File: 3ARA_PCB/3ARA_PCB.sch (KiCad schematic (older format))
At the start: 45 parts, among them J1 ST-LINK V2, SW1 SW_SPST, SW2 SW_SPST, U1 STM32F407VGTx, Y1 8MHz

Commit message: Continuacion del esquematico
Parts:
- added C20: 100uF, Capacitor_SMD:CP_Elec_6.3x5.4, symbol Device:CP
- added C21: 1000uF, symbol Device:CP
- added D4: MBR360, Diode_SMD:D_SMA_Handsoldering, symbol Diode:MBR340
- added J12: JUMP_1, Connector_PinHeader_2.54mm:PinHeader_1x02_P2.54mm_Vertical, symbol Connector:Conn_01x02_Male
- added J13: JUMP_2, Connector_PinHeader_2.54mm:PinHeader_1x02_P2.54mm_Vertical, symbol Connector:Conn_01x02_Male
- added J14: SPI 1, Connector_JST:JST_EH_B4B-EH-A_1x04_P2.50mm_Vertical, symbol Connector:Conn_01x04_Male
- added J15: UART 5, Connector_JST:JST_EH_B4B-EH-A_1x04_P2.50mm_Vertical, symbol Connector:Conn_01x04_Male
- added J9: DC Input, symbol Connector:Conn_01x02_Male
- added L1: 100uH, Inductor_THT:L_Axial_L7.0mm_D3.3mm_P12.70mm_Horizontal_Fastron_MICC, symbol pspice:INDUCTOR
- added R10, R11, R8, R9: 1K, Resistor_SMD:R_0805_2012Metric_Pad1.20x1.40mm_HandSolder, symbol Device:R_Small
- added U3: LM2576S-3.3, Package_TO_SOT_SMD:TO-263-5_TabPin3, symbol Regulator_Switching:LM2576S-3.3
- C1, C10, C11, C12, C13, C14, C15, C16, C17, C18, C19, C2, C4, C6, C7, C8, C9: footprint (none) -> Capacitor_SMD:C_0805_2012Metric_Pad1.18x1.45mm_HandSolder
- C3, C5: footprint (none) -> Capacitor_THT:C_Disc_D5.0mm_W2.5mm_P5.00mm
- D1, D2: footprint (none) -> LED_SMD:LED_0805_2012Metric_Pad1.15x1.40mm_HandSolder
- D3: renamed from D?; footprint (none) -> LED_SMD:LED_0805_2012Metric_Pad1.15x1.40mm_HandSolder
- J1: footprint (none) -> Connector_PinHeader_2.54mm:PinHeader_2x05_P2.54mm_Vertical
- J10: renamed from J?; value Hall 2 -> Encoder 2; footprint (none) -> Connector_JST:JST_EH_B4B-EH-A_1x04_P2.50mm_Vertical
- J11: renamed from J?; value Hall 3 -> Encoder 3; footprint (none) -> Connector_JST:JST_EH_B4B-EH-A_1x04_P2.50mm_Vertical
- J2, J4, J6: renamed from J?; footprint (none) -> Connector_JST:JST_EH_B3B-EH-A_1x03_P2.50mm_Vertical
- J3, J5, J7: renamed from J?; footprint (none) -> Connector_PinHeader_2.54mm:PinHeader_1x03_P2.54mm_Vertical
- J8: renamed from J?; value Hall 1 -> Encoder 1; footprint (none) -> Connector_JST:JST_EH_B4B-EH-A_1x04_P2.50mm_Vertical
- R1, R2, R3, R4, R5: footprint (none) -> Resistor_SMD:R_0805_2012Metric_Pad1.20x1.40mm_HandSolder
- R6: renamed from R?; value 2K -> 1K; footprint (none) -> Resistor_SMD:R_0805_2012Metric_Pad1.20x1.40mm_HandSolder
- R7: renamed from R?; footprint (none) -> Resistor_SMD:R_0805_2012Metric_Pad1.20x1.40mm_HandSolder
- SW1: value SW_SPST -> RESET; footprint (none) -> Button_Switch_THT:SW_PUSH_6mm
- SW2: value SW_SPST -> BTN; footprint (none) -> Button_Switch_THT:SW_PUSH_6mm
- SW3: renamed from SW?; footprint (none) -> Button_Switch_THT:SW_PUSH_6mm
- U2: renamed from U?; footprint XCVR_HC-05 -> HC05:XCVR_HC-05
- Y1: footprint (none) -> Crystal:Crystal_HC49-U_Vertical
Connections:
- net +3V3: now also C21.1, J15.1 (Pin_1), L1.2, R10.2, R8.2, R9.2, U3.4 (FB)
- net GND: now also C20.2, C21.2, D4.2 (A), J14.4 (Pin_4), J15.4 (Pin_4), J9.2 (Pin_2), U3.3 (GND), U3.5 (~ON~/OFF)
- net HALL_1: now also R8.1
- net HALL_2: now also U1.87 (PD6), R9.1; no longer U1.90 (PB4)
- net HALL_3: now also U1.86 (PD5), R10.1; no longer U1.91 (PB5)
- net MOTOR_2_L: now also U1.3 (PE4)
- net MOTOR_2_R: now also U1.1 (PE2)
- net PA2(Tx): now also J12.1 (Pin_1); no longer U2.2 (UART-RX)
- net PA3(Rx): now also J12.2 (Pin_2); no longer U2.1 (UART-TX)
- net PA5_SPI_1_SCK: now reaches U1.30 (PA5)
- net PA5_SPI_1_SCK: now also J14.3 (Pin_3)
- net PC12_UART_5_Tx: now reaches U1.80 (PC12)
- net PC12_UART_5_Tx: now also J15.3 (Pin_3)
- net PD2_UART_5_Rx: now reaches U1.83 (PD2)
- net PD2_UART_5_Rx: now also J15.2 (Pin_2)
- net at R6.2: now also R11.1; no longer D3.2 (A)
- new net: D3.2 (A), R11.2
- new net: D4.1 (K), L1.1, U3.2 (OUT)
- new net +12V: C20.1, J9.1 (Pin_1), U3.1 (VIN)
- new net HC05_RX: J13.2 (Pin_2), U2.2 (UART-RX)
- new net HC05_TX: J13.1 (Pin_1), U2.1 (UART-TX)
- new net PB4_SPI_1_MISO: J14.2 (Pin_2), U1.90 (PB4)
- new net PB5_SPI_1_MOSI: J14.1 (Pin_1), U1.91 (PB5)
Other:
- note added: "JUMPER"
- note added: "Power Supply"
- moved on the sheet: C18, C19, D1, D2, D3, J1, J10, J11, J8, R2, R3, R4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

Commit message: Avance con el PCB
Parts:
- removed C14: 100nF, Capacitor_SMD:C_0805_2012Metric_Pad1.18x1.45mm_HandSolder, symbol Device:C
- removed C15: 1uF, Capacitor_SMD:C_0805_2012Metric_Pad1.18x1.45mm_HandSolder, symbol Device:C
- added D5, D6: LED, LED_SMD:LED_0805_2012Metric_Pad1.15x1.40mm_HandSolder, symbol Device:LED
- added J16: GPIO, Connector_PinHeader_2.54mm:PinHeader_2x05_P2.54mm_Vertical, symbol Connector_Generic:Conn_02x05_Counter_Clockwise
- added L2: 100uH - optional, Inductor_THT:L_Axial_L7.0mm_D3.3mm_P12.70mm_Horizontal_Fastron_MICC, symbol pspice:INDUCTOR
- added R12, R13, R14: 1K, Resistor_SMD:R_0805_2012Metric_Pad1.20x1.40mm_HandSolder, symbol Device:R_Small
- C18, C19: value 0.1uF -> 100nF
- C21: footprint (none) -> Capacitor_THT:CP_Radial_D10.0mm_P7.50mm
- J1: footprint Connector_PinHeader_2.54mm:PinHeader_2x05_P2.54mm_Vertical -> Connector_IDC:IDC-Header_2x05_P2.54mm_Vertical
- J14: value SPI 1 -> I2C 1
- J3: value Hall 1 -> Hall 3; footprint Connector_PinHeader_2.54mm:PinHeader_1x03_P2.54mm_Vertical -> Connector_JST:JST_EH_B3B-EH-A_1x03_P2.50mm_Vertical
- J5: footprint Connector_PinHeader_2.54mm:PinHeader_1x03_P2.54mm_Vertical -> Connector_JST:JST_EH_B3B-EH-A_1x03_P2.50mm_Vertical
- J7: value Hall 3 -> Hall 1; footprint Connector_PinHeader_2.54mm:PinHeader_1x03_P2.54mm_Vertical -> Connector_JST:JST_EH_B3B-EH-A_1x03_P2.50mm_Vertical
- J9: footprint (none) -> Connector_JST:JST_EH_B2B-EH-A_1x02_P2.50mm_Vertical
- L1: footprint Inductor_THT:L_Axial_L7.0mm_D3.3mm_P12.70mm_Horizontal_Fastron_MICC -> Inductor_SMD:L_12x12mm_H6mm
- R1: value 47 -> 120
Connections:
- net +3V3: now also C16.2, C17.2, J14.1 (Pin_1), U1.21 (VREF+), U1.22 (VDDA), J16.10 (Pin_10), L2.2, R12.1, R13.1, R14.1; no longer J1.8 (Pin_8), R1.2
- net GND: now also J1.5 (Pin_5), D5.1 (K), D6.1 (K), J16.6 (Pin_6)
- net HALL_1: now also J7.1 (Pin_1), R10.1; no longer J3.1 (Pin_1), R8.1
- net HALL_3: now also J3.1 (Pin_1), R8.1; no longer J7.1 (Pin_1), R10.1
- net MOTOR_1_L: now also U1.18 (PC3)
- net MOTOR_1_R: now also U1.29 (PA4); no longer U1.18 (PC3)
- net NRST: now also J1.1 (Pin_1)
- net TIM3_CH1: now also U1.31 (PA6)
- net TIM3_CH2: now also U1.32 (PA7)
- net PE7: now reaches U1.38 (PE7)
- net PE7: now also J16.1 (Pin_1)
- net PE10: now reaches U1.41 (PE10)
- net PE10: now also J16.2 (Pin_2)
- net PE11: now reaches U1.42 (PE11)
- net PE11: now also J16.3 (Pin_3)
- net PB12: now reaches U1.51 (PB12)
- net PB12: now also J16.4 (Pin_4)
- net PB13: now reaches U1.52 (PB13)
- net PB13: now also J16.5 (Pin_5)
- net PB14: now reaches U1.53 (PB14)
- net PB14: now also J16.9 (Pin_9)
- net PB6_I2C1_SCL: now reaches U1.92 (PB6)
- net PB6_I2C1_SCL: now also J14.3 (Pin_3), R13.2
- net PB7_I2C1_SDA: now reaches U1.93 (PB7)
- net PB7_I2C1_SDA: now also J14.2 (Pin_2), R12.2
- net at J1.7 (Pin_7): now also R1.2
- net at D4.1 (K), L1.1, U3.2 (OUT): now also L2.1
- net PA5_SPI_1_SCK: no longer names the net of U1.30 (PA5)
- net PA5_SPI_1_SCK: no longer J14.3 (Pin_3)
- net PB4_SPI_1_MISO: no longer names the net of U1.90 (PB4)
- net PB4_SPI_1_MISO: no longer J14.2 (Pin_2)
- net PB5_SPI_1_MOSI: no longer names the net of U1.91 (PB5)
- net PB5_SPI_1_MOSI: no longer J14.1 (Pin_1)
- removed net VREF+: C16.2, C17.2, R1.1, U1.21 (VREF+), U1.22 (VDDA)
- new net: D5.2 (A), R1.1
- new net: D6.2 (A), R14.2
- no-connect marks 0 -> 3
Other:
- moved on the sheet: J3, J7, R10, R8

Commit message: Agregado de gpios a pines
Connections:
- net +3V3: now also J16.2 (Pin_2); no longer J16.10 (Pin_10)
- net GND: now also J16.1 (Pin_1), J16.9 (Pin_9); no longer J16.6 (Pin_6)
- net PB13: now also J16.6 (Pin_6); no longer J16.5 (Pin_5)
- net PB14: now also J16.8 (Pin_8); no longer J16.9 (Pin_9)
- net PE0: no longer D1.2 (A)
- net PE7: no longer J16.1 (Pin_1)
- net PC1: now reaches U1.16 (PC1)
- net PC1: now also D1.2 (A)
- net PE8: now reaches U1.39 (PE8)
- net PE8: now also C19.2, R3.1, SW2.1 (A)
- net PB15: now reaches U1.54 (PB15)
- net PB15: now also J16.10 (Pin_10)
- net PA10: now reaches U1.69 (PA10)
- net PA10: now also J16.7 (Pin_7)
- net PA11: now reaches U1.70 (PA11)
- net PA11: now also J16.5 (Pin_5)
- net PA12: now reaches U1.71 (PA12)
- net PA12: now also J16.3 (Pin_3)
- removed net PD15: C19.2, R3.1, SW2.1 (A), U1.62 (PD15)
- net PE10: no longer names the net of U1.41 (PE10)
- net PE10: no longer J16.2 (Pin_2)
- net PE11: no longer names the net of U1.42 (PE11)
- net PE11: no longer J16.3 (Pin_3)
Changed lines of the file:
@@
 $EndComp
 Text Label 9875 1200 1    50   ~ 0
-PE0
+PC1
 Wire Wire Line
 	9875 1750 9875 1925
@@
 Wire Wire Line
 	2850 7850 3425 7850
-Text Label 9100 1625 0    50   ~ 0
-PD15
 Wire Wire Line
 	8850 1625 9100 1625
-Text Label 2850 8050 0    50   ~ 0
-PD15
-Wire Wire Line
-	2850 8050 3425 8050
 Text Label 5725 3250 0    50   ~ 0
 MOTOR_1(PWM)
@@
 Text Label 2875 5550 0    50   ~ 0
 PE7
-Text Label 2875 5850 0    50   ~ 0
-PE10
-Wire Wire Line
-	2875 5850 3425 5850
 Wire Wire Line
 	2875 5550 3425 5550
-Text Label 2875 5950 0    50   ~ 0
-PE11
-Wire Wire Line
-	3425 5950 2875 5950
-Text Label 13100 4100 0    50   ~ 0
-PE7
-Text Label 13100 4200 0    50   ~ 0
-PE10
-Text Label 13100 4300 0    50   ~ 0
-PE11
+Text Label 14175 4100 0    50   ~ 0
+PB15
 Text Label 5725 6050 0    50   ~ 0
 PB12
@@
 Wire Wire Line
 	5225 6250 5725 6250
-Text Label 13100 4400 0    50   ~ 0
+Text Label 12950 4400 0    50   ~ 0
 PB12
-Text Label 13100 4500 0    50   ~ 0
+Text Label 14175 4500 0    50   ~ 0
 PB13
-Text Label 14075 4200 0    50   ~ 0
+Text Label 14175 4300 0    50   ~ 0
 PB14
 $Comp
@@
 L power:GND #PWR0103
 U 1 1 614D4ACB
-P 14075 4575
-F 0 "#PWR0103" H 14075 4325 50  0001 C CNN
-F 1 "GND" H 14080 4402 50  0000 C CNN
-F 2 "" H 14075 4575 50  0001 C CNN
-F 3 "" H 14075 4575 50  0001 C CNN
-	1    14075 4575
+P 14575 4650
+F 0 "#PWR0103" H 14575 4400 50  0001 C CNN
+F 1 "GND" H 14580 4477 50  0000 C CNN
+F 2 "" H 14575 4650 50  0001 C CNN
+F 3 "" H 14575 4650 50  0001 C CNN
+	1    14575 4650
 	1    0    0    -1
 $EndComp
@@
 L power:+3.3V #PWR0104
 U 1 1 614D4DF5
-P 14075 4000
-F 0 "#PWR0104" H 14075 3850 50  0001 C CNN
-F 1 "+3.3V" H 14090 4173 50  0000 C CNN
-F 2 "" H 14075 4000 50  0001 C CNN
-F 3 "" H 14075 4000 50  0001 C CNN
-	1    14075 4000
-	1    0    0    -1
-$EndComp
-Wire Wire Line
-	13875 4100 14075 4100
-Wire Wire Line
-	14075 4100 14075 4000
-Wire Wire Line
-	13875 4500 14075 4500
-Wire Wire Line
-	14075 4500 14075 4575
-Wire Wire Line
-	13100 4500 13375 4500
-Wire Wire Line
-	13100 4400 13375 4400
-Wire Wire Line
-	13100 4300 13375 4300
-Wire Wire Line
-	13100 4200 13375 4200
-Wire Wire Line
-	13100 4100 13375 4100
-Wire Wire Line
-	13875 4200 14075 4200
+P 12950 4025
+F 0 "#PWR0104" H 12950 3875 50  0001 C CNN
+F 1 "+3.3V" H 12965 4198 50  0000 C CNN
+F 2 "" H 12950 4025 50  0001 C CNN
+F 3 "" H 12950 4025 50  0001 C CNN
+	1    12950 4025
+	1    0    0    -1
+$EndComp
 $Comp
 L Device:LED D6
@@
 Wire Wire Line
 	5225 3850 5725 3850
+Text Label 2875 5650 0    50   ~ 0
+PE8
+Wire Wire Line
+	2875 5650 3425 5650
+Text Label 9100 1625 0    50   ~ 0
+PE8
+Text Label 5725 6650 0    50   ~ 0
+PC1
+Wire Wire Line
+	5225 6650 5725 6650
+Wire Wire Line
+	12950 4025 12950 4200
+Wire Wire Line
+	12950 4200 13375 4200
+Text Label 5725 4350 0    50   ~ 0
+PA12
+Text Label 5725 4250 0    50   ~ 0
+PA11
+Text Label 5725 4150 0    50   ~ 0
+PA10
+Wire Wire Line
+	5225 4150 5725 4150
+Wire Wire Line
+	5725 4250 5225 4250
+Wire Wire Line
+	5225 4350 5725 4350
+Wire Wire Line
+	13875 4200 14575 4200
+Wire Wire Line
+	14575 4200 14575 4650
+Text Label 12950 4300 0    50   ~ 0
+PA12
+Wire Wire Line
+	13875 4400 14175 4400
+Text Label 12950 4500 0    50   ~ 0
+PA11
+Wire Wire Line
+	12950 4300 13375 4300
+Text Label 14175 4400 0    50   ~ 0
+PA10
+Wire Wire Line
+	12950 4500 13375 4500
+Wire Wire Line
+	13875 4100 14175 4100
+Wire Wire Line
+	14175 4300 13875 4300
+Wire Wire Line
+	12950 4400 13375 4400
+Wire Wire Line
+	14175 4500 13875 4500
+Text Label 5725 6350 0    50   ~ 0
+PB15
+Wire Wire Line
+	5225 6350 5725 6350
+Wire Wire Line
+	13375 4100 13225 4100
+Wire Wire Line
+	13225 4100 13225 3750
+Wire Wire Line
+	13225 3750 14575 3750
+Wire Wire Line
+	14575 3750 14575 4200
+Connection ~ 14575 4200
 $EndSCHEMATC

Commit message: Generación de la BOM
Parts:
- added C14, C22, C25, C27: 100nF, Capacitor_SMD:C_0805_2012Metric_Pad1.18x1.45mm_HandSolder, symbol Device:C
- added C15, C23, C24, C26: 1uF, Capacitor_SMD:C_0805_2012Metric_Pad1.18x1.45mm_HandSolder, symbol Device:C
- added D7: MBR360, Diode_SMD:D_SMA_Handsoldering, symbol Diode:MBR340
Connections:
- net +12V: now also D7.1 (K); no longer J9.1 (Pin_1)
- net +3V3: now also C14.2, C15.2, C22.2, C23.2, C24.1, C25.1, C26.1, C27.1
- net GND: now also C14.1, C15.1, C22.1, C23.1, C24.2, C25.2, C26.2, C27.2
- net HC05_TX: now also J12.2 (Pin_2); no longer J13.1 (Pin_1)
- net PA2(Tx): now also J13.1 (Pin_1); no longer J12.1 (Pin_1)
- net PA3(Rx): now also J12.1 (Pin_1); no longer J12.2 (Pin_2)
- new net: D7.2 (A), J9.1 (Pin_1)
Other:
- moved on the sheet: J10, J11, J8, J9

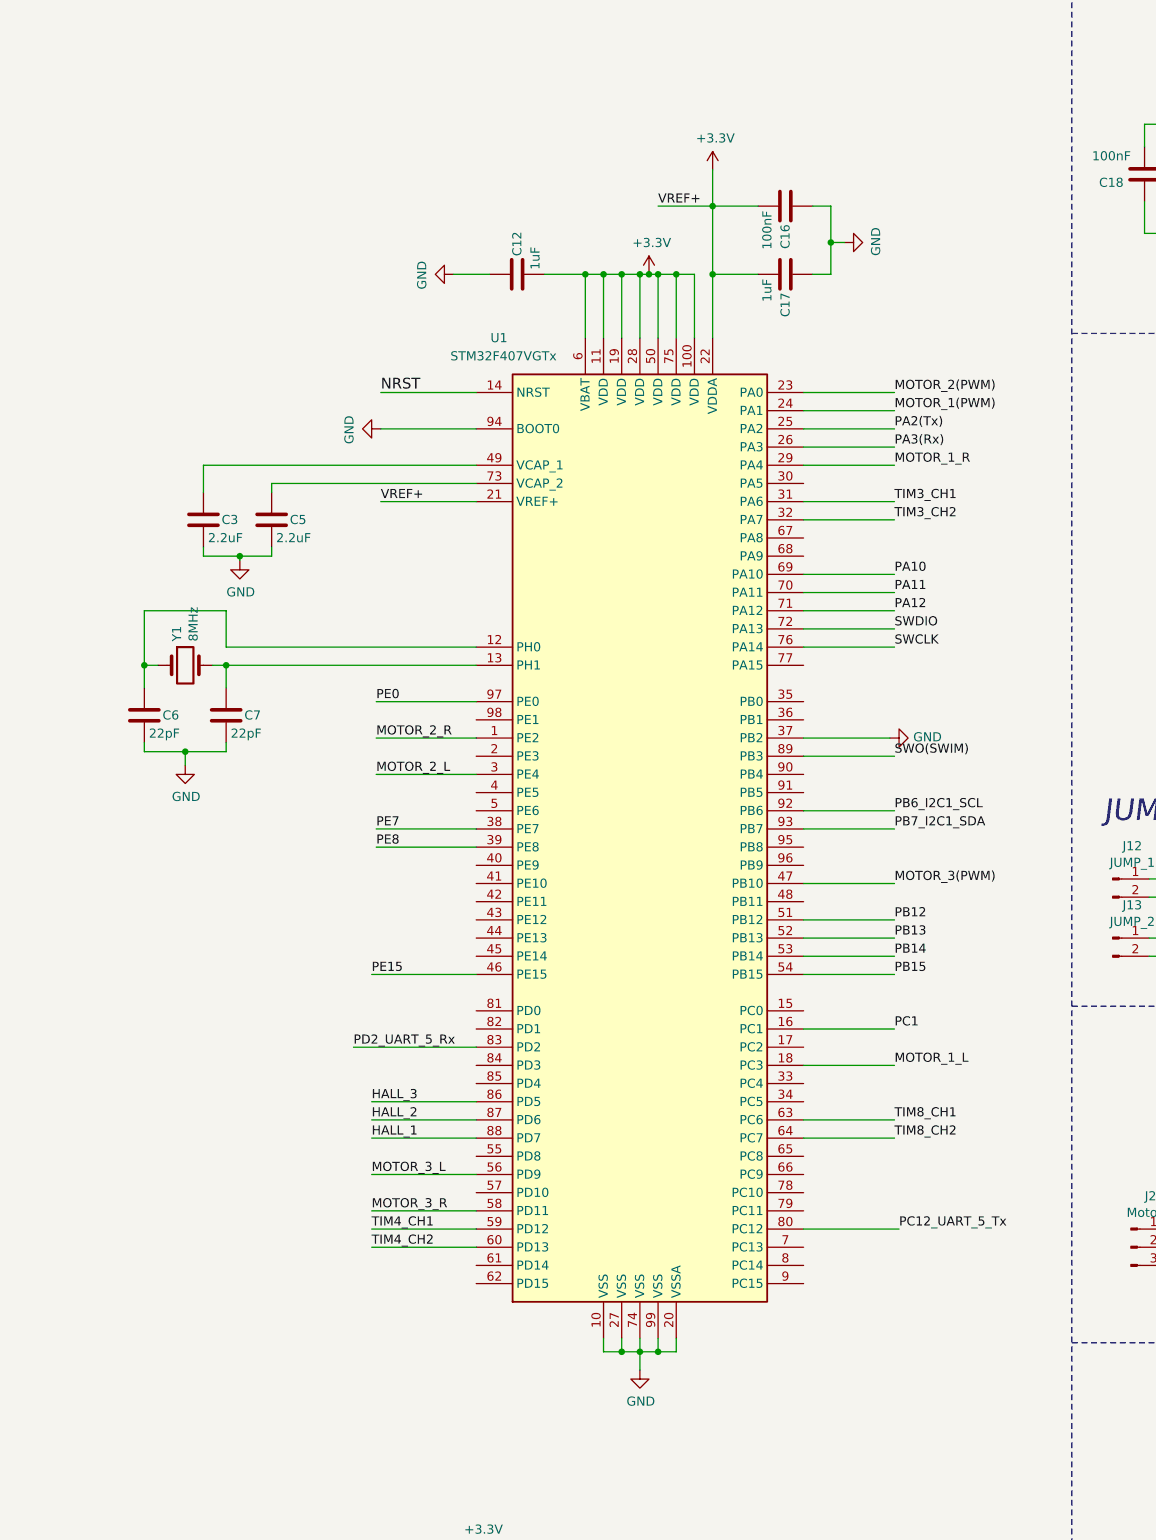
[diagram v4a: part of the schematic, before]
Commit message: Agregado de R pull down a boot 0 y capacitores en alimentacion
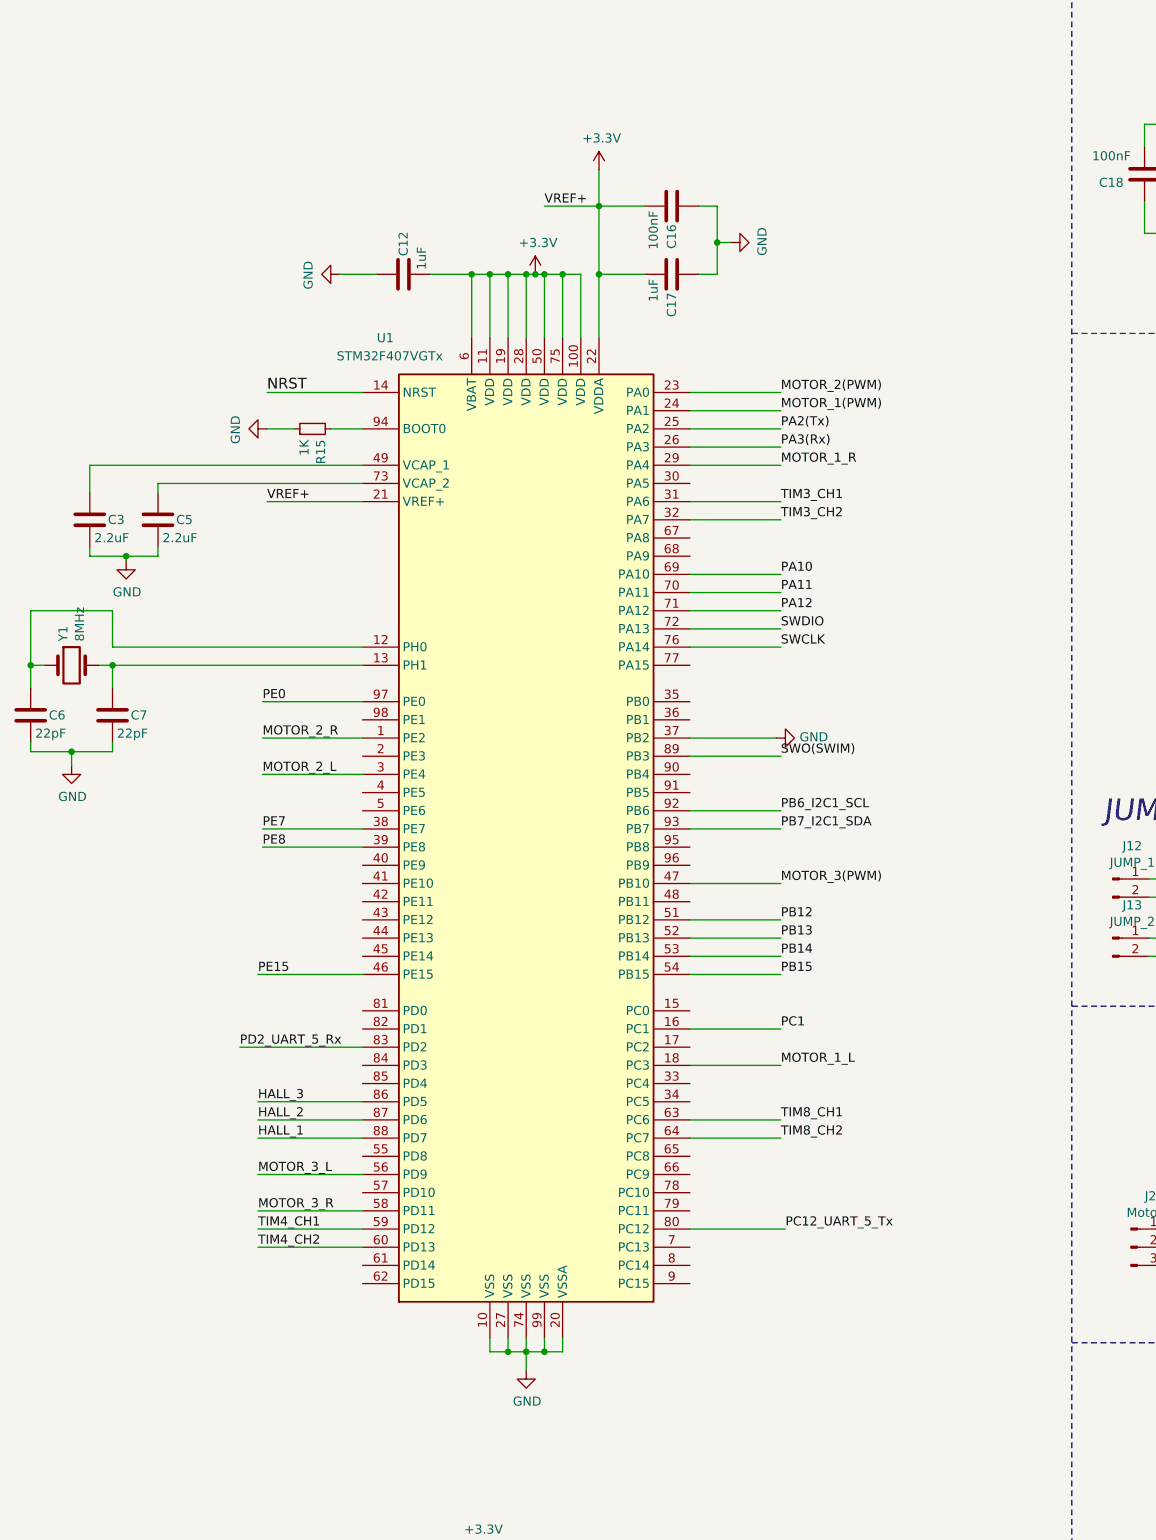
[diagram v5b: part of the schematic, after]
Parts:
- added R15: 1K, Resistor_SMD:R_0805_2012Metric_Pad1.20x1.40mm_HandSolder, symbol Device:R_Small
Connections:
- net GND: now also R15.1; no longer U1.94 (BOOT0)
- new net: R15.2, U1.94 (BOOT0)
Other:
- moved on the sheet: C12, C16, C17, C3, C5, C6, C7, U1, Y1
